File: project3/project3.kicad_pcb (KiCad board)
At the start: 2 copper layers, 1 part

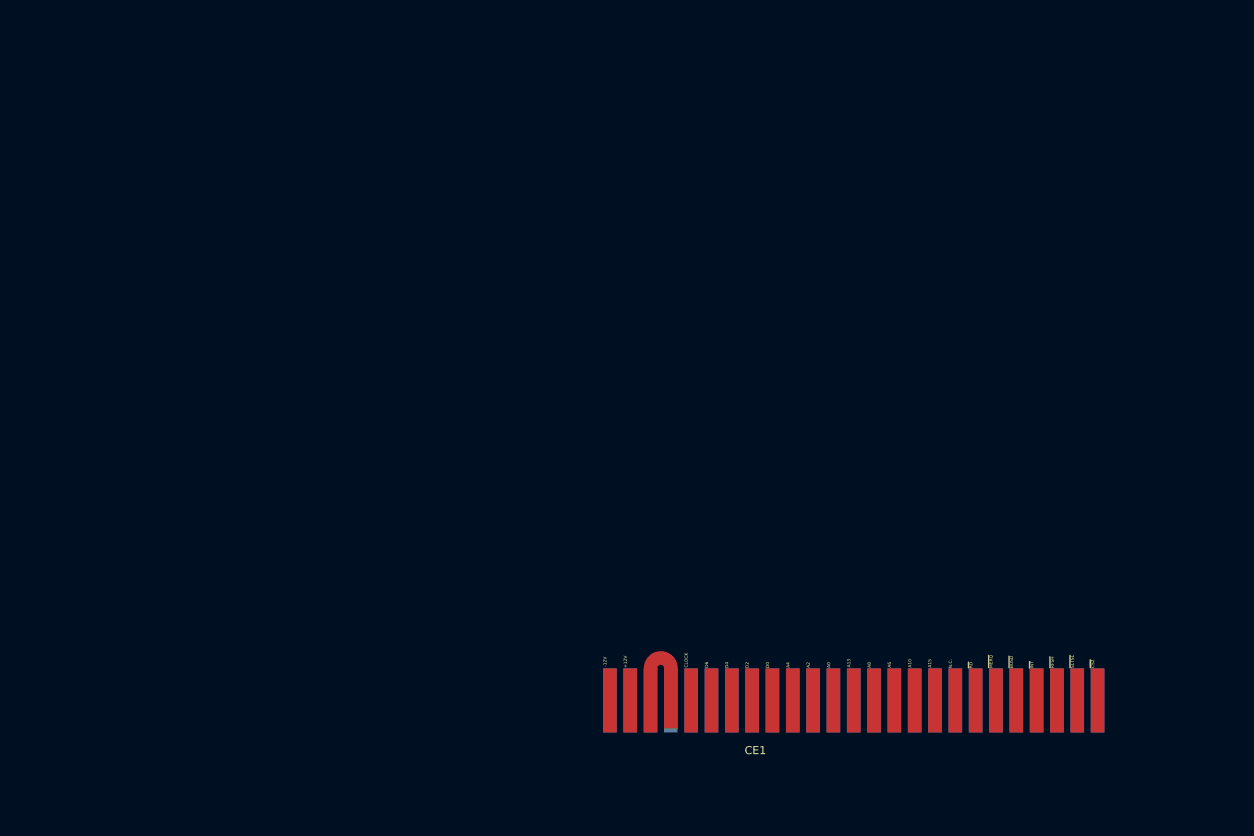
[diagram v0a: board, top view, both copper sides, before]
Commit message: Created 4Mega ROM PCB - Change DIP32 type FLASH ROM - Optimal Logic Mega Rom Mapper.
Signed-off-by: Youngki Park <ykp7409@gmail.com>
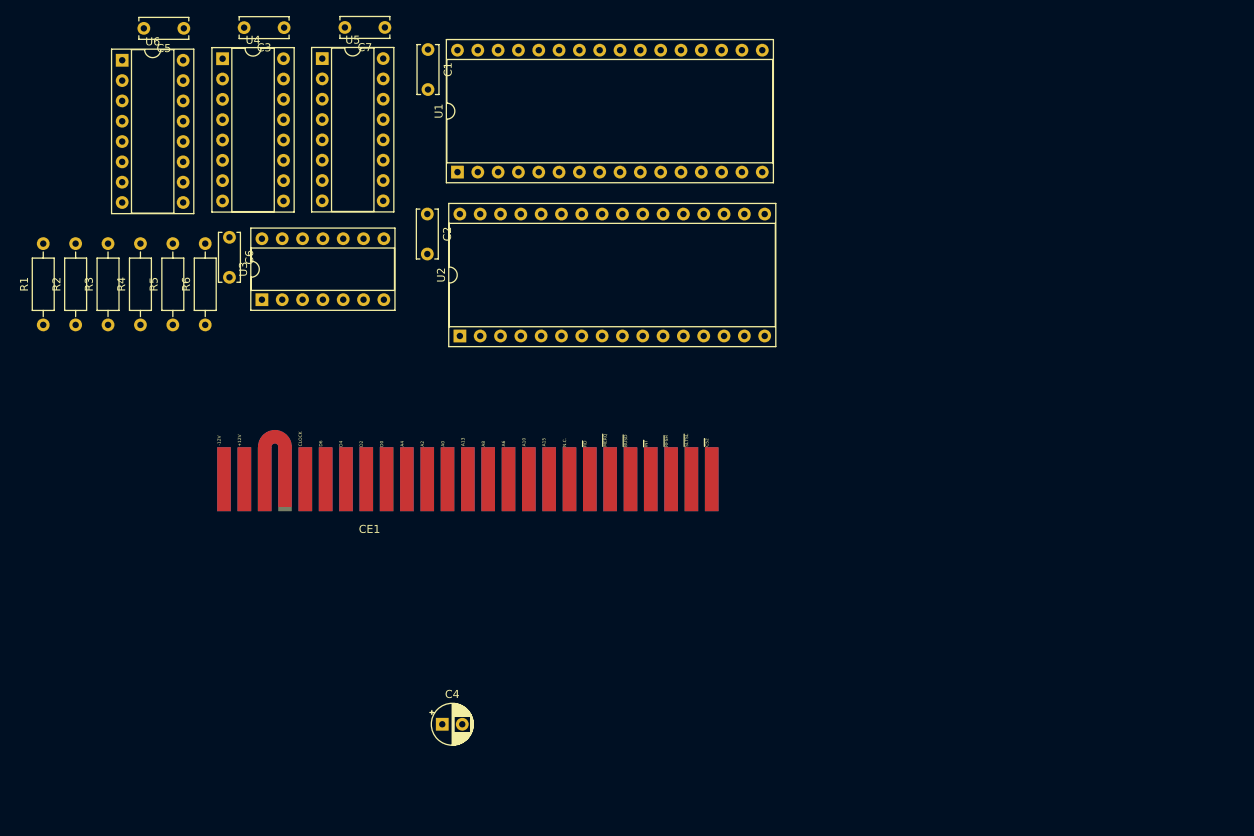
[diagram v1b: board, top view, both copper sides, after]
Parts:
- added C1: 100n, Capacitor_THT:C_Disc_D6.0mm_W2.5mm_P5.00mm, F.Cu at (89.0, 35.5)
- added C2: 100n, Capacitor_THT:C_Disc_D6.0mm_W2.5mm_P5.00mm, F.Cu at (88.9, 56.0)
- added C3: 100n, Capacitor_THT:C_Disc_D6.0mm_W2.5mm_P5.00mm, F.Cu at (71.0, 32.7)
- added C4: 10uf, Capacitor_THT:CP_Radial_D5.0mm_P2.50mm, F.Cu at (90.8, 119.8)
- added C5: 100n, Capacitor_THT:C_Disc_D6.0mm_W2.5mm_P5.00mm, F.Cu at (58.5, 32.8)
- added C6: 100n, Capacitor_THT:C_Disc_D6.0mm_W2.5mm_P5.00mm, F.Cu at (64.2, 59.0)
- added C7: 100n, Capacitor_THT:C_Disc_D6.0mm_W2.5mm_P5.00mm, F.Cu at (83.6, 32.7)
- added R1: 470R, Resistor_THT:R_Axial_DIN0207_L6.3mm_D2.5mm_P10.16mm_Horizontal, F.Cu at (40.9, 69.9)
- added R2: 470R, Resistor_THT:R_Axial_DIN0207_L6.3mm_D2.5mm_P10.16mm_Horizontal, F.Cu at (45.0, 69.9)
- added R3: 470R, Resistor_THT:R_Axial_DIN0207_L6.3mm_D2.5mm_P10.16mm_Horizontal, F.Cu at (49.0, 69.9)
- added R4: 470R, Resistor_THT:R_Axial_DIN0207_L6.3mm_D2.5mm_P10.16mm_Horizontal, F.Cu at (53.1, 69.9)
- added R5: 470R, Resistor_THT:R_Axial_DIN0207_L6.3mm_D2.5mm_P10.16mm_Horizontal, F.Cu at (57.1, 69.9)
- added R6: 470R, Resistor_THT:R_Axial_DIN0207_L6.3mm_D2.5mm_P10.16mm_Horizontal, F.Cu at (61.2, 69.9)
- added U1: SST27ST020, Package_DIP:DIP-32_W15.24mm_Socket, F.Cu at (92.7, 50.8)
- added U2: SST27ST020, Package_DIP:DIP-32_W15.24mm_Socket, F.Cu at (93.0, 71.3)
- added U3: 74LS02, Package_DIP:DIP-14_W7.62mm_Socket, F.Cu at (68.3, 66.7)
- added U4: 74LS670, Package_DIP:DIP-16_W7.62mm_Socket, F.Cu at (63.3, 36.6)
- added U5: 74LS139, Package_DIP:DIP-16_W7.62mm_Socket, F.Cu at (75.8, 36.6)
- added U6: 74LS670, Package_DIP:DIP-16_W7.62mm_Socket, F.Cu at (50.8, 36.8)
- moved CE1 55.6 mm to (92.8, 86.0)
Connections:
- CE1 pad 13: unconnected-(CE1-~{WR}-Pad13) -> //WR
- CE1 pad 14: unconnected-(CE1-~{RD}-Pad14) -> //RD
- CE1 pad 17: unconnected-(CE1-A9-Pad17) -> /A9
- CE1 pad 18: unconnected-(CE1-A15-Pad18) -> /A15
- CE1 pad 19: unconnected-(CE1-A11-Pad19) -> /A11
- CE1 pad 20: unconnected-(CE1-A10-Pad20) -> /A10
- CE1 pad 21: unconnected-(CE1-A7-Pad21) -> /A7
- CE1 pad 22: unconnected-(CE1-A6-Pad22) -> /A6
- CE1 pad 23: unconnected-(CE1-A12-Pad23) -> /A12
- CE1 pad 24: unconnected-(CE1-A8-Pad24) -> /A8
- CE1 pad 26: unconnected-(CE1-A13-Pad26) -> /A13
- CE1 pad 27: unconnected-(CE1-A1-Pad27) -> /A1
- CE1 pad 28: unconnected-(CE1-A0-Pad28) -> /A0
- CE1 pad 29: unconnected-(CE1-A3-Pad29) -> /A3
- CE1 pad 30: unconnected-(CE1-A2-Pad30) -> /A2
- CE1 pad 31: unconnected-(CE1-A5-Pad31) -> /A5
- CE1 pad 32: unconnected-(CE1-A4-Pad32) -> /A4
- CE1 pad 33: unconnected-(CE1-D1-Pad33) -> /D1
- CE1 pad 34: unconnected-(CE1-D0-Pad34) -> /D0
- CE1 pad 35: unconnected-(CE1-D3-Pad35) -> /D3
- CE1 pad 36: unconnected-(CE1-D2-Pad36) -> /D2
- CE1 pad 37: unconnected-(CE1-D5-Pad37) -> /D5
- CE1 pad 38: unconnected-(CE1-D4-Pad38) -> /D4
- CE1 pad 39: unconnected-(CE1-D7-Pad39) -> /D7
- CE1 pad 4: unconnected-(CE1-~{STLSL}-Pad4) -> //SLTSL
- CE1 pad 40: unconnected-(CE1-D6-Pad40) -> /D6
- CE1 pad 41: unconnected-(CE1-GND-Pad41) -> GND
- CE1 pad 43: unconnected-(CE1-GND-Pad43) -> GND
- CE1 pad 45: unconnected-(CE1-+5V-Pad45) -> +5V
- CE1 pad 47: unconnected-(CE1-+5V-Pad47) -> +5V

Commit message: Modify PCB design.
Signed-off-by: ykp74 <ykp7409@gmail.com>
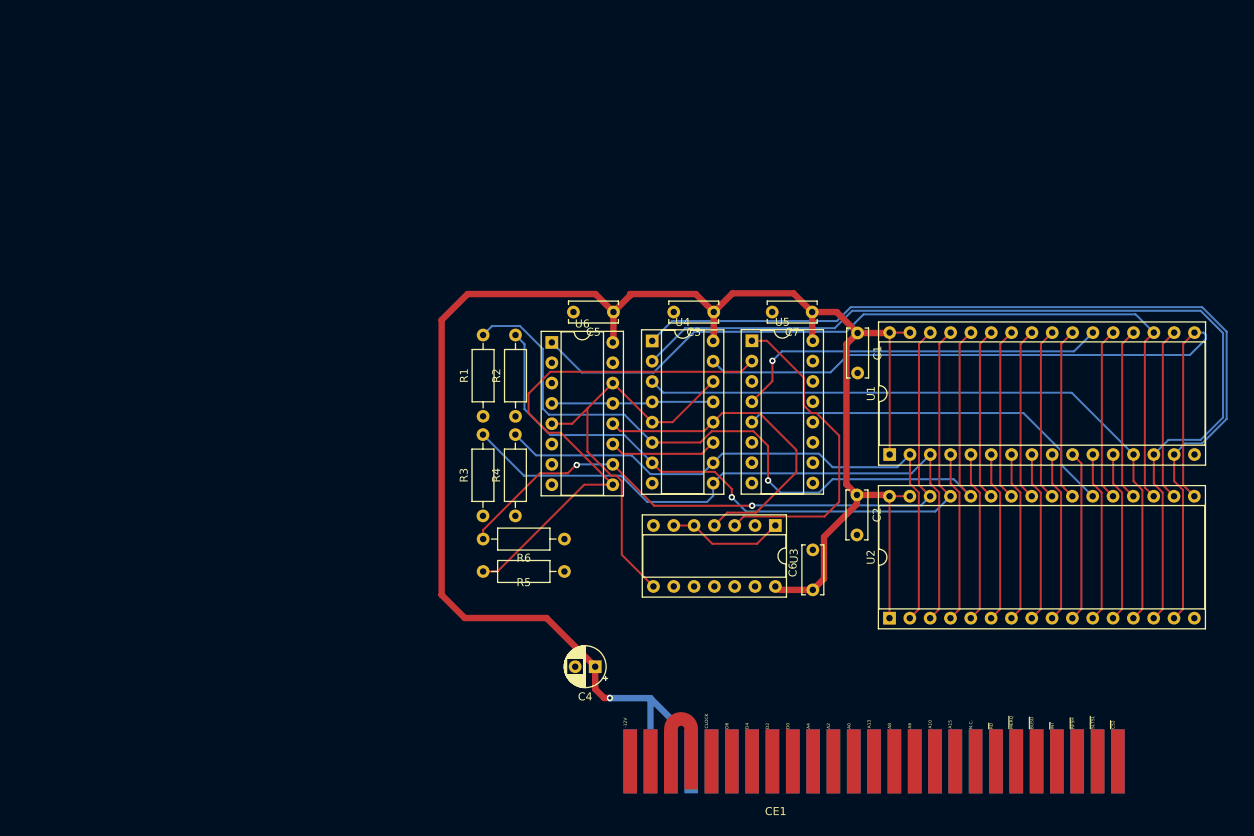
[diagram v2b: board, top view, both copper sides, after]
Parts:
- moved C6 85.2 mm to (137.1, 103.0), turned to 90 degrees
- moved U3 70.1 mm to (132.4, 95.0), turned to -90 degrees
- moved U1 64.5 mm to (146.7, 86.1)
- moved C3 64.4 mm to (124.7, 68.3)
- moved C5 64.4 mm to (112.2, 68.3)
- moved C1 64.3 mm to (142.7, 70.9)
- moved U4 64.3 mm to (117.0, 71.9)
- moved U6 64.3 mm to (104.5, 72.1)
- moved U2 64.3 mm to (146.7, 106.6)
- moved U5 64.3 mm to (129.5, 71.9)
- moved C7 64.2 mm to (137.1, 68.3)
- moved C2 64.2 mm to (142.6, 91.2)
- moved CE1 61.8 mm to (143.5, 121.3)
- moved R5 57.8 mm to (106.1, 100.7), turned to 180 degrees
- moved R1 56.2 mm to (95.9, 81.3)
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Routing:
- net +5V: track 0.00 -> 238.5 mm, vias 0 -> 1
- net /D1: track 0.00 -> 117.6 mm
- net /D2: track 0.00 -> 115.5 mm
- net /D5: track 0.00 -> 102.1 mm
- net /MA13: track 0.00 -> 102.0 mm, vias 0 -> 1
- net /MA14: track 0.00 -> 91.3 mm, vias 0 -> 1
- net /D3: track 0.00 -> 87.6 mm
- net /D0: track 0.00 -> 85.3 mm
- net /MA17: track 0.00 -> 85.0 mm, vias 0 -> 2
- net /MA15: track 0.00 -> 84.2 mm
- net /MA16: track 0.00 -> 75.2 mm
- net Net-(U5A-A0): track 0.00 -> 67.0 mm
- net /A15: track 0.00 -> 52.4 mm
- net /ROM_CE2: track 0.00 -> 48.4 mm
- net /ROM_CE1: track 0.00 -> 47.7 mm, vias 0 -> 1
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
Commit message: Modify the PCB layout
Signed-off-by: Youngki Park <ykp7409@gmail.com>
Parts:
- C1, C2, C3, C5, C6, C7: value 100n -> 0.1uF
- C4: value 10uf -> 10uF
- R1, R2, R3, R4, R5, R6: value 470R -> 470
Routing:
- net /D4: track 21.6 -> 176.3 mm, vias 0 -> 2
- net /A13: track 20.2 -> 96.1 mm, vias 0 -> 1
- net /D3: track 87.6 -> 159.7 mm
- net /A15: track 52.4 -> 122.7 mm, vias 0 -> 4
- net /D5: track 102.1 -> 172.3 mm
- net /D6: track 21.6 -> 90.0 mm, vias 0 -> 1
- net /D2: track 115.5 -> 183.9 mm, vias 0 -> 1
- net /D7: track 21.6 -> 88.7 mm
- net /D1: track 117.6 -> 182.3 mm
- net /D0: track 85.3 -> 146.1 mm, vias 0 -> 1
- net //SLTSL: track 40.4 -> 95.5 mm, vias 0 -> 3
- net //WR: track 0.00 -> 55.0 mm, vias 0 -> 2
- net /A0: track 21.4 -> 67.8 mm, vias 0 -> 1
- net /A4: track 21.4 -> 67.6 mm, vias 0 -> 1
- net /A1: track 21.4 -> 66.4 mm
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- added copper zone on B.Cu, net GND
- added copper zone on F.Cu, net GND
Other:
- board outline added: 100.8 x 64 mm
- board text added: "4 Mega Rom Pack Ver 1.1 Designed by supers02"
- board text added: "Youngki Park"

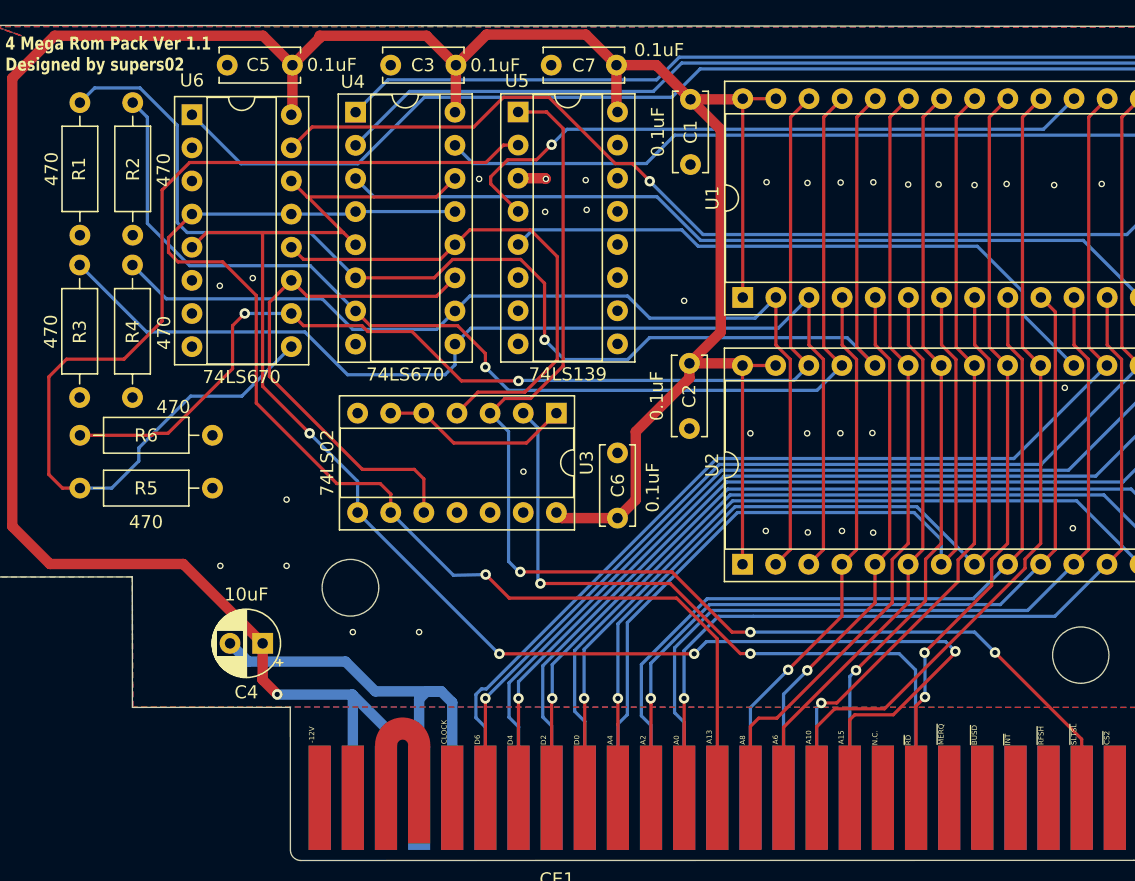
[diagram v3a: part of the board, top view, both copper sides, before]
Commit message: Modified PCB some design Optimal layout.
Signed-off-by: ykp74 <ykp7409@gmail.com>
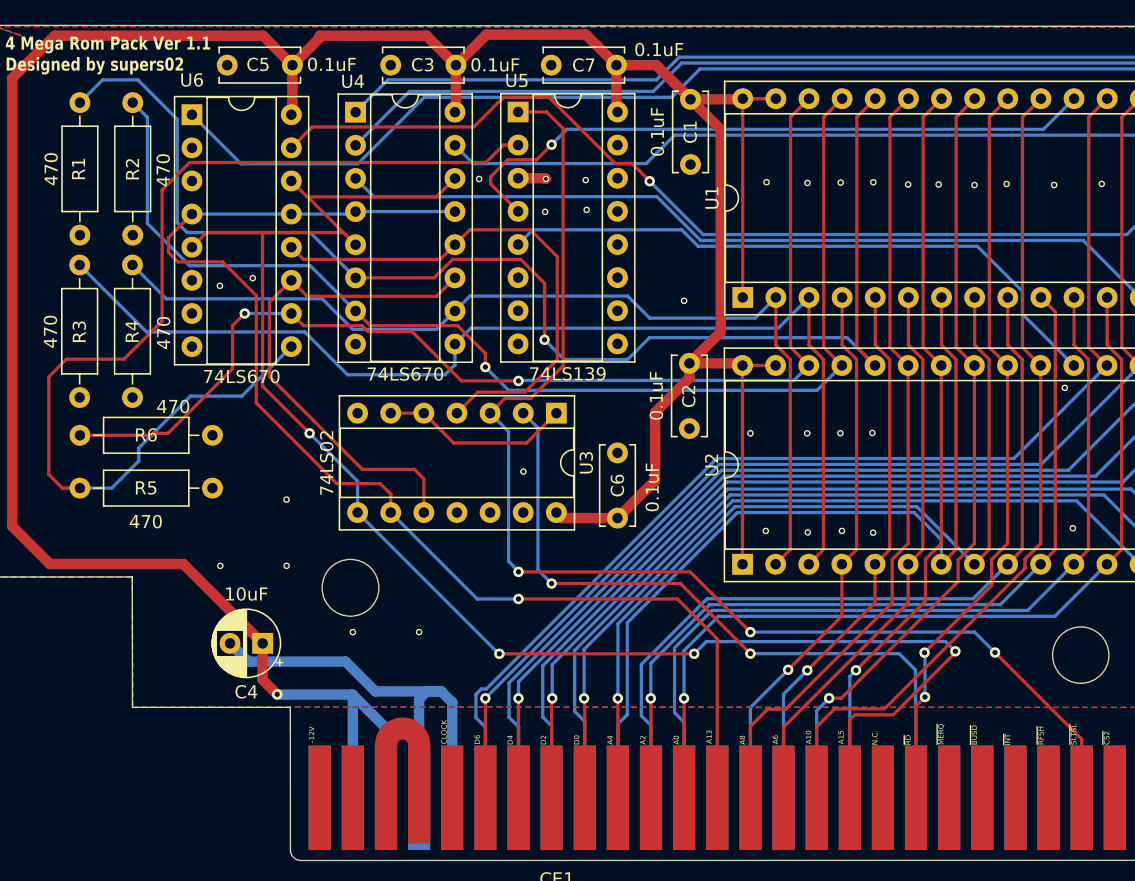
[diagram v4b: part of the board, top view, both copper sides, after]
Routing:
- net /MA13: track 101.3 -> 102.1 mm
- net //WR: track 55.0 -> 54.4 mm

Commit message: Build gerber files
Signed-off-by: Youngki Park <ykp7409@gmail.com>
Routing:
- net GND: vias 50 -> 55
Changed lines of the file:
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@@
   (via (at 148.499983 104.004626) (size 0.5) (drill 0.3) (layers "F.Cu" "B.Cu") (free) (net 22))
   (via (at 185.197401 75.543019) (size 0.5) (drill 0.3) (layers "F.Cu" "B.Cu") (free) (net 22))
+  (via (at 137.052367 95.208839) (size 0.8) (drill 0.4) (layers "F.Cu" "B.Cu") (free) (net 22))
   (via (at 154.340587 104.004626) (size 0.5) (drill 0.3) (layers "F.Cu" "B.Cu") (free) (net 22))
   (via (at 182.88 111.76) (size 0.5) (drill 0.3) (layers "F.Cu" "B.Cu") (free) (net 22))
@@
   (via (at 161.747583 77.443832) (size 0.5) (drill 0.3) (layers "F.Cu" "B.Cu") (free) (net 22))
   (via (at 111.76 101.6) (size 0.5) (drill 0.3) (layers "F.Cu" "B.Cu") (free) (net 22))
+  (via (at 142.24 86.36) (size 0.8) (drill 0.4) (layers "F.Cu" "B.Cu") (free) (net 22))
+  (via (at 140.456723 86.293952) (size 0.8) (drill 0.4) (layers "F.Cu" "B.Cu") (free) (net 22))
   (via (at 177.8 111.76) (size 0.5) (drill 0.3) (layers "F.Cu" "B.Cu") (free) (net 22))
   (via (at 187.96 101.6) (size 0.5) (drill 0.3) (layers "F.Cu" "B.Cu") (free) (net 22))
   (via (at 182.171032 100.111587) (size 0.5) (drill 0.3) (layers "F.Cu" "B.Cu") (free) (net 22))
+  (via (at 142.249784 84.236702) (size 0.8) (drill 0.4) (layers "F.Cu" "B.Cu") (free) (net 22))
   (via (at 131.583164 79.539681) (size 0.5) (drill 0.3) (layers "F.Cu" "B.Cu") (free) (net 22))
   (via (at 187.96 116.84) (size 0.5) (drill 0.3) (layers "F.Cu" "B.Cu") (free) (net 22))
   (via (at 147.32 96.52) (size 0.5) (drill 0.3) (layers "F.Cu" "B.Cu") (free) (net 22))
+  (via (at 135.244629 95.133007) (size 0.8) (drill 0.4) (layers "F.Cu" "B.Cu") (free) (net 22))
   (via (at 164.50303 77.486223) (size 0.5) (drill 0.3) (layers "F.Cu" "B.Cu") (free) (net 22))
   (via (at 177.262866 77.316657) (size 0.5) (drill 0.3) (layers "F.Cu" "B.Cu") (free) (net 22))
@@
   (via (at 174.253071 77.40144) (size 0.5) (drill 0.3) (layers "F.Cu" "B.Cu") (free) (net 22))
   (via (at 156.733351 104.13651) (size 0.5) (drill 0.3) (layers "F.Cu" "B.Cu") (free) (net 22))
+  (via (at 140.434708 82.705384) (size 0.8) (drill 0.4) (layers "F.Cu" "B.Cu") (free) (net 22))
   (via (at 185.253923 79.979994) (size 0.5) (drill 0.3) (layers "F.Cu" "B.Cu") (free) (net 22))
   (via (at 109.166967 84.621076) (size 0.5) (drill 0.3) (layers "F.Cu" "B.Cu") (free) (net 22))
@@
   (via (at 187.96 111.76) (size 0.5) (drill 0.3) (layers "F.Cu" "B.Cu") (free) (net 22))
   (via (at 187.96 106.68) (size 0.5) (drill 0.3) (layers "F.Cu" "B.Cu") (free) (net 22))
-  (via (at 142.24 86.36) (size 0.5) (drill 0.3) (layers "F.Cu" "B.Cu") (free) (net 22))
   (via (at 156.745388 77.274266) (size 0.5) (drill 0.3) (layers "F.Cu" "B.Cu") (free) (net 22))
   (via (at 154.220565 96.513021) (size 0.5) (drill 0.3) (layers "F.Cu" "B.Cu") (free) (net 22))
